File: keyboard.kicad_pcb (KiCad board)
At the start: 2 copper layers, 285 x 94.6 mm, 319 parts, among them IC1 ATMEGA32U4, J1 USBTYPEC, P1 DIL16, P2 DIL16, P3 CONN_6, SW1 SW_PUSH, U1 USBLC6-2SC6, X1 ASX4

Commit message: add a 100n capacitor for VBUS-GND
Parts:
- added C15: 100n, 0805:0805C, B.Cu at (76.1, 78.3)
- moved F1 0.29 mm to (78.2, 78.3)
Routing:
- net GND: track 1418.1 -> 1421.4 mm, vias 98 -> 96
- net Net-(C15-Pad1): track 21.1 -> 24.2 mm, vias 2 -> 4

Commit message: fix mounting holes on row5
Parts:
- removed the REF** at (325.4, 150.0)
- removed the REF** at (165.4, 150.0)
- removed the REF** at (155.4, 150.0)
- removed the REF** at (115.5, 150.0)
- removed the REF** at (105.5, 150.0)
- removed the REF** at (85.5, 150.0)
- removed the REF** at (95.5, 150.0)
- removed the REF** at (315.4, 150.0)
- removed the REF** at (305.4, 150.0) (x2)
- removed the REF** at (255.4, 150.0)
- removed the REF** at (245.4, 150.0)
- removed the REF** at (235.4, 150.0)
- removed the REF** at (225.4, 150.0)
- removed the REF** at (175.4, 150.0)
- added REF**: MountingHole_2.5mm, Mounting_Holes:MountingHole_2.5mm, F.Cu at (247.7, 150.0)
- added REF**: MountingHole_2.5mm, Mounting_Holes:MountingHole_2.5mm, F.Cu at (176.2, 150.0)
- added REF**: MountingHole_2.5mm, Mounting_Holes:MountingHole_2.5mm, F.Cu at (95.2, 150.0)
- added REF**: MountingHole_2.5mm, Mounting_Holes:MountingHole_2.5mm, F.Cu at (85.7, 150.0)
- added REF**: MountingHole_2.5mm, Mounting_Holes:MountingHole_2.5mm, F.Cu at (327.4, 150.0)
- added REF**: MountingHole_2.5mm, Mounting_Holes:MountingHole_2.5mm, F.Cu at (328.6, 150.0)
- added REF**: MountingHole_2.5mm, Mounting_Holes:MountingHole_2.5mm, F.Cu at (142.9, 150.0)
- added REF**: MountingHole_2.5mm, Mounting_Holes:MountingHole_2.5mm, F.Cu at (309.6, 150.0)
- added REF**: MountingHole_2.5mm, Mounting_Holes:MountingHole_2.5mm, F.Cu at (323.9, 150.0)
- added REF**: MountingHole_2.5mm, Mounting_Holes:MountingHole_2.5mm, F.Cu at (223.8, 150.0)
- added REF**: MountingHole_2.5mm, Mounting_Holes:MountingHole_2.5mm, F.Cu at (238.1, 150.0)
- added REF**: MountingHole_2.5mm, Mounting_Holes:MountingHole_2.5mm, F.Cu at (252.4, 150.0)
- added REF**: MountingHole_2.5mm, Mounting_Holes:MountingHole_2.5mm, F.Cu at (181.0, 150.0)
- added REF**: MountingHole_2.5mm, Mounting_Holes:MountingHole_2.5mm, F.Cu at (166.7, 150.0)
- moved R1 1.14 mm to (71.0, 67.0)
- moved R2 1.09 mm to (90.0, 67.0)
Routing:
- net GND: track 1421.4 -> 1423.9 mm
- net Net-(J1-PadA5): track 12.2 -> 11.1 mm
- net Net-(J1-PadB5): track 10.2 -> 11.3 mm

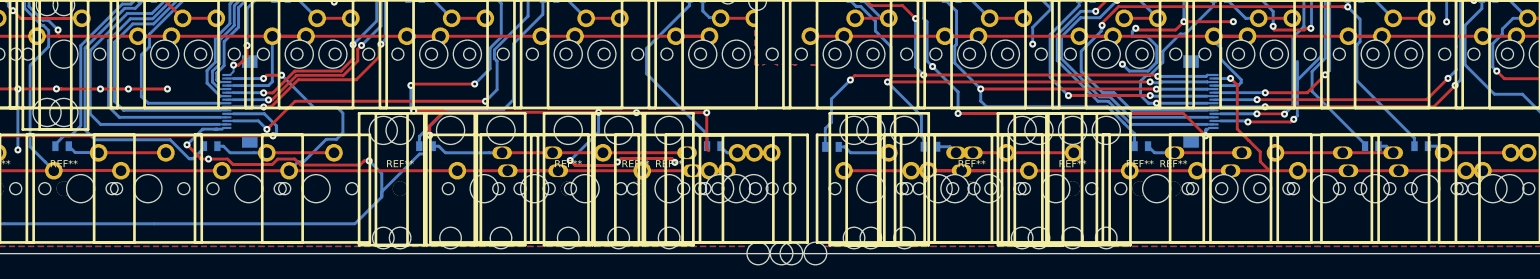
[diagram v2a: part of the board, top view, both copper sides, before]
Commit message: support hhkb layout
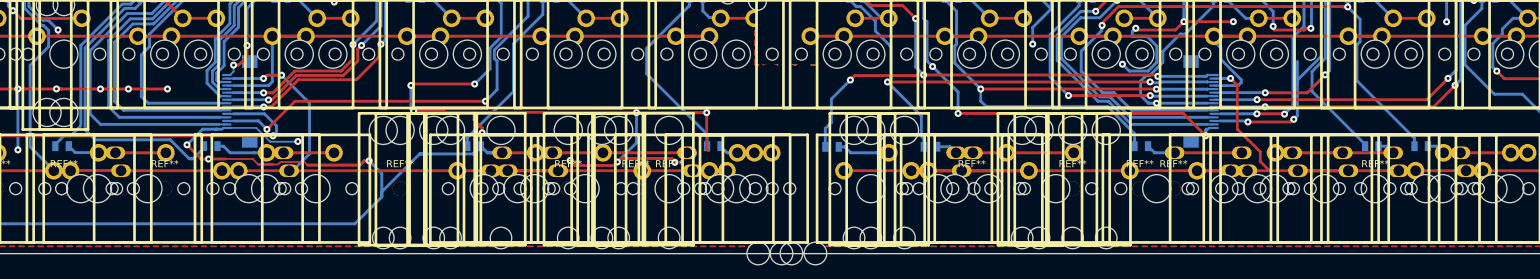
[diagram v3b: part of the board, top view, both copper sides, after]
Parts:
- added MXST: VAL**, mx1a:MXST, F.Cu at (171.4, 150.0)
- added MXST: VAL**, mx1a:MXST, F.Cu at (147.6, 150.0)
- added REF**: MountingHole_2.5mm, Mounting_Holes:MountingHole_2.5mm, F.Cu at (281.0, 150.0)
- added REF**: MountingHole_2.5mm, Mounting_Holes:MountingHole_2.5mm, F.Cu at (109.5, 150.0)
- added S102: MX1A, mx1a:MX1A_no3d, F.Cu at (100.0, 150.0)
- added S152: MX1A, mx1a:MX1A_no3d, F.Cu at (123.8, 150.0)
- added S304: MX1A, mx1a:MX1A_no3d, F.Cu at (159.5, 150.0)
- added S553: MX1A, mx1a:MX1A_no3d, F.Cu at (266.7, 150.0)
- added S603: MX1A, mx1a:MX1A_no3d, F.Cu at (290.5, 150.0)
- moved D30 6.80 mm to (153.3, 144.0)
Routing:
- net GND: track 1423.9 -> 1441.3 mm
- net /col6: track 182.5 -> 174.9 mm
- net /row5-r: track 288.1 -> 292.8 mm
- net Net-(D30-Pad2): track 37.4 -> 34.8 mm
- net Net-(D60-Pad2): track 14.5 -> 16.9 mm
- net Net-(D55-Pad2): track 19.1 -> 21.5 mm
- net Net-(D15-Pad2): track 16.9 -> 19.3 mm
- net Net-(D10-Pad2): track 14.1 -> 16.5 mm

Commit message: change atmega32u4 footprint to QFN-44
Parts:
- IC1: footprint tqfp:TQFP44 -> Housings_DFN_QFN:QFN-44-1EP_7x7mm_Pitch0.5mm
- moved IC1 2.21 mm to (90.8, 102.5)
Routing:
- net VCC: track 362.4 -> 415.3 mm, vias 11 -> 19
- net GND: track 1441.3 -> 1476.1 mm, vias 96 -> 99
- net /col3: track 146.5 -> 162.6 mm, vias 3 -> 5
- net /row2: track 200.5 -> 211.1 mm, vias 6 -> 8
- net /col7: track 381.1 -> 387.9 mm
- net /row3: track 157.0 -> 162.9 mm, vias 5 -> 4
- net Net-(IC1-Pad33): track 14.7 -> 19.6 mm
- net /col4: track 110.8 -> 115.7 mm
- net /row5: track 211.9 -> 216.4 mm, vias 4 -> 2
- net /col6: track 174.9 -> 179.3 mm
- net /col5: track 131.5 -> 135.3 mm
- net /row4: track 176.5 -> 180.1 mm, vias 3 -> 1
- net Net-(C8-Pad1): track 8.80 -> 12.0 mm
- net Net-(C6-Pad1): track 8.64 -> 11.5 mm
- net /CapsLED: track 66.3 -> 69.1 mm, vias 3 -> 4
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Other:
- net class Default: trace_width 0.4064 -> 0.254

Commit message: cleanup DRC warnings and adjust LEDs/reset_button position
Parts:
- moved C10 24.8 mm to (215.0, 119.8)
- moved R12 15.1 mm to (82.2, 100.5), turned to 0 degrees
- moved LED2 14.3 mm to (220.5, 119.8)
- moved C12 13.3 mm to (258.5, 119.8)
- moved C11 8.57 mm to (120.9, 119.8)
- moved C9 8.51 mm to (86.8, 119.8)
- moved LED3 8.24 mm to (126.4, 119.8)
- moved LED1 8.19 mm to (92.3, 119.8)
- moved C14 7.93 mm to (302.0, 119.8)
- moved R13 6.27 mm to (85.6, 113.2)
- moved SW1 4.17 mm to (91.4, 112.8), turned to 0 degrees
- moved LED4 3.11 mm to (264.0, 119.8)
- moved LED6 3.11 mm to (307.5, 119.8)
- moved LED5 2.52 mm to (160.5, 119.8)
- moved C13 1.82 mm to (155.0, 119.8)
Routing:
- net GND: track 1476.1 -> 1189.0 mm, vias 99 -> 73
- net /VCC-r: track 111.0 -> 138.7 mm, vias 5 -> 9
- net /col9: track 88.4 -> 61.7 mm
- net /col8: track 124.6 -> 99.5 mm
- net Net-(LED3-Pad2): track 21.9 -> 35.4 mm
- net /row2: track 211.1 -> 198.2 mm, vias 8 -> 6
- net Net-(IC1-Pad33): track 19.6 -> 7.49 mm
- net /GPIO0: track 58.1 -> 47.3 mm
- net Net-(LED2-Pad2): track 31.3 -> 41.7 mm
- net /col11: track 82.9 -> 88.7 mm
- net Net-(LED4-Pad2): track 35.8 -> 41.4 mm
- net /row1: track 498.2 -> 503.5 mm
- net /row4: track 180.1 -> 175.2 mm
- net VCC: track 415.3 -> 410.8 mm, vias 19 -> 23
- net /row5: track 216.4 -> 220.8 mm
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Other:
- board text added: "."

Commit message: cleanup and generate production_files
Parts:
- DW9: moved to B.Cu
- moved R5 10.9 mm to (64.8, 107.7), turned to 270 degrees
- moved C15 9.26 mm to (85.3, 79.3), turned to 90 degrees
- moved DW9 5.67 mm to (64.8, 111.9)
- moved F1 2.00 mm to (78.2, 80.3)
- moved U1 1.50 mm to (81.0, 79.6)
- moved R10 1.24 mm to (80.4, 83.7)
- moved R11 1.20 mm to (83.3, 83.7)
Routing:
- net GND: track 1189.0 -> 1237.4 mm, vias 73 -> 82
- net /CapsLED: track 69.1 -> 58.3 mm, vias 4 -> 2
- net Net-(C15-Pad1): track 24.2 -> 32.2 mm, vias 4 -> 5
- net Net-(DW9-Pad2): track 9.07 -> 2.32 mm, vias 1 -> 0
- net /row1: track 503.5 -> 500.0 mm
- net /col1: track 109.8 -> 107.6 mm
- net /col9: track 61.7 -> 63.6 mm
- net Net-(J1-PadA6): track 9.99 -> 11.5 mm
- net Net-(J1-PadA7): track 8.74 -> 10.2 mm
- net Net-(IC1-Pad13): track 68.4 -> 66.9 mm
- net Net-(IC1-Pad3): track 19.4 -> 18.5 mm
- net /col8: track 99.5 -> 98.8 mm
- net /col14: track 133.4 -> 132.8 mm
- net VCC: track 410.8 -> 410.7 mm, vias 23 -> 22
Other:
- board text removed: "."

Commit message: change ISP pinout connector to 2.0mm x 6
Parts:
- P3: footprint Connectors_Molex:Molex_KK-6410-06_06x2.54mm_Straight -> Connectors_Molex:Molex_MicroLatch-53253-0670_06x2.00mm_Straight
- moved P3 2.71 mm to (64.0, 94.2)
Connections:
- IC1 pad 45: GND -> (no net)
- J1 pad B9: Net-(C15-Pad1) -> (no net)
- P3 pad 1: Net-(IC1-Pad13) -> VCC
- P3 pad 2: VCC -> GND
- P3 pad 3: GND -> Net-(IC1-Pad13)
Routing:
- net Net-(IC1-Pad13): track 66.9 -> 72.8 mm, vias 4 -> 5
- net /CapsLED: track 58.3 -> 62.4 mm
- net (no net): track 0.00 -> 3.86 mm
- net /col8: track 98.8 -> 100.7 mm
- net GND: track 1237.4 -> 1236.1 mm, vias 82 -> 83
- net VCC: track 410.7 -> 411.3 mm

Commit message: cleanup trackes
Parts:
- added REF**: MountingHole_2.5mm, Mounting_Holes:MountingHole_2.5mm, F.Cu at (214.3, 135.9)
- added REF**: MountingHole_2.5mm, Mounting_Holes:MountingHole_2.5mm, F.Cu at (219.1, 135.9)
- added REF**: MountingHole_2.5mm, Mounting_Holes:MountingHole_2.5mm, F.Cu at (181.0, 135.9)
- added REF**: MountingHole_2.5mm, Mounting_Holes:MountingHole_2.5mm, F.Cu at (104.8, 135.9)
- added REF**: MountingHole_2.5mm, Mounting_Holes:MountingHole_2.5mm, F.Cu at (100.0, 135.9)
- added REF**: MountingHole_2.5mm, Mounting_Holes:MountingHole_2.5mm, F.Cu at (176.2, 135.9)
- added REF**: MountingHole_2.5mm, Mounting_Holes:MountingHole_2.5mm, F.Cu at (295.3, 135.9)
- added REF**: MountingHole_2.5mm, Mounting_Holes:MountingHole_2.5mm, F.Cu at (328.6, 135.9)
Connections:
- IC1 pad 45: (no net) -> GND
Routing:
- net GND: track 1236.1 -> 1350.0 mm, vias 83 -> 90
- net /col10: track 90.5 -> 80.2 mm
- net /GPIO0: track 47.3 -> 37.8 mm
- net /col14: track 132.9 -> 127.5 mm
- net /col13: track 87.5 -> 82.1 mm
- net /col8-r: track 122.3 -> 126.3 mm
- net (no net): track 3.86 -> 0.00 mm
- net VCC: track 411.3 -> 407.5 mm
- net /col11: track 88.7 -> 85.4 mm
- net /GPIO0-r: track 76.1 -> 79.3 mm
- net /col12: track 87.4 -> 84.4 mm
- net /col3: track 161.9 -> 159.0 mm
- net /col1: track 107.6 -> 109.8 mm
- net /GPIO0_out: track 57.9 -> 59.3 mm
- net /col14-r: track 203.2 -> 204.6 mm
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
